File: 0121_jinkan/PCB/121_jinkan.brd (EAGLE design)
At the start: 25.4 x 33 mm, 16 parts

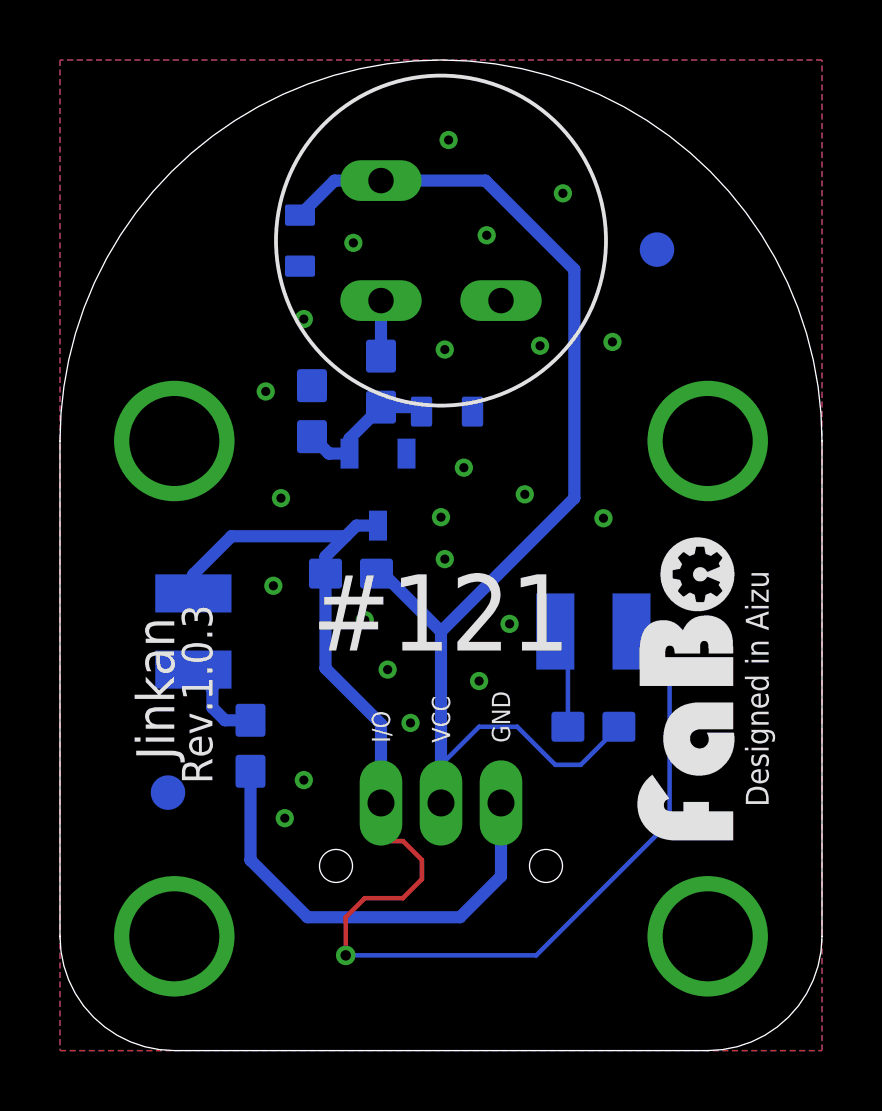
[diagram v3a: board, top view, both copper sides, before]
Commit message: #0121 Jinkan 配線太さ変更修正
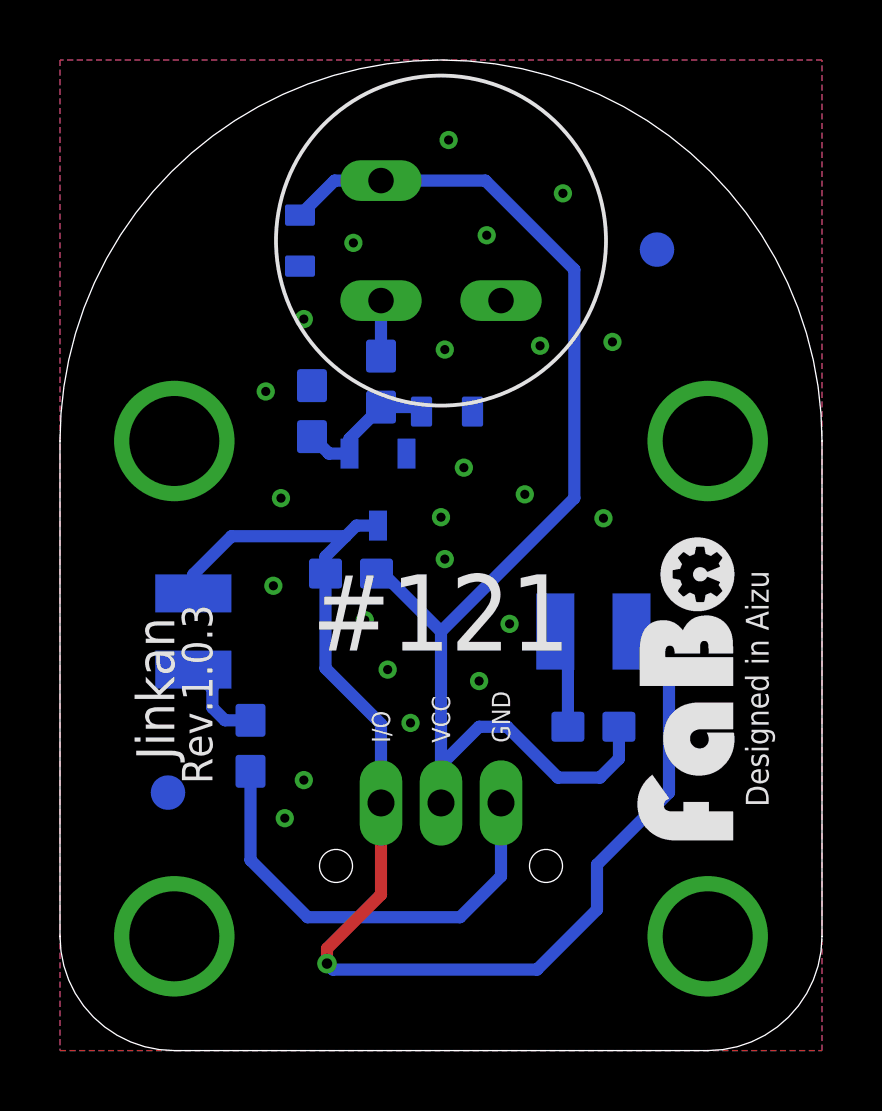
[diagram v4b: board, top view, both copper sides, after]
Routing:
- net VCC: track 42.2 -> 43.2 mm
- net I/O: track 44.7 -> 44.2 mm
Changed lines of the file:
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@@
 <rectangle x1="15.5" y1="15.3" x2="17.2" y2="15.6" layer="42"/>
 <rectangle x1="18.3" y1="15.3" x2="19.9" y2="15.6" layer="42"/>
-<rectangle x1="15.8" y1="12.4" x2="16.8" y2="12.6" layer="42"/>
+<rectangle x1="15.6" y1="12.4" x2="16.6" y2="12.6" layer="42"/>
 <rectangle x1="18.5" y1="12.3" x2="19.5" y2="12.6" layer="42"/>
 </plain>
@@
 <wire x1="5.715" y1="17.145" x2="9.525" y2="17.145" width="0.4064" layer="16"/>
 <contactref element="SJ2" pad="1"/>
-<wire x1="19.05" y1="13.97" x2="20.32" y2="12.7" width="0.1524" layer="16"/>
-<wire x1="15.875" y1="3.175" x2="9.525" y2="3.175" width="0.1524" layer="16"/>
-<via x="9.525" y="3.175" extent="1-16" drill="0.35"/>
-<wire x1="9.525" y1="3.175" x2="9.525" y2="4.445" width="0.1524" layer="1"/>
-<wire x1="9.525" y1="4.445" x2="10.16" y2="5.08" width="0.1524" layer="1"/>
-<wire x1="10.16" y1="5.08" x2="11.43" y2="5.08" width="0.1524" layer="1"/>
-<wire x1="11.43" y1="5.08" x2="12.065" y2="5.715" width="0.1524" layer="1"/>
-<wire x1="12.065" y1="5.715" x2="12.065" y2="6.35" width="0.1524" layer="1"/>
-<wire x1="12.065" y1="6.35" x2="11.43" y2="6.985" width="0.1524" layer="1"/>
-<wire x1="11.43" y1="6.985" x2="10.795" y2="6.985" width="0.1524" layer="1"/>
-<wire x1="10.795" y1="6.985" x2="10.7" y2="7.08" width="0.1524" layer="1"/>
-<wire x1="10.7" y1="7.08" x2="10.7" y2="8.255" width="0.1524" layer="1"/>
-<wire x1="20.32" y1="12.7" x2="20.32" y2="7.62" width="0.1524" layer="16"/>
-<wire x1="20.32" y1="7.62" x2="15.875" y2="3.175" width="0.1524" layer="16"/>
+<wire x1="19.05" y1="13.97" x2="20.3" y2="12.72" width="0.4064" layer="16"/>
+<wire x1="17.9" y1="4.7" x2="15.9" y2="2.7" width="0.4064" layer="16"/>
+<wire x1="15.9" y1="2.7" x2="9.1" y2="2.7" width="0.4064" layer="16"/>
+<wire x1="9.1" y1="2.7" x2="8.9" y2="2.9" width="0.4064" layer="16"/>
+<via x="8.9" y="2.9" extent="1-16" drill="0.35"/>
+<wire x1="8.9" y1="2.9" x2="8.9" y2="3.4" width="0.4064" layer="1"/>
+<wire x1="20.3" y1="12.72" x2="20.3" y2="8.6" width="0.4064" layer="16"/>
+<wire x1="20.3" y1="8.6" x2="17.9" y2="6.2" width="0.4064" layer="16"/>
+<wire x1="17.9" y1="6.2" x2="17.9" y2="4.7" width="0.4064" layer="16"/>
+<wire x1="8.9" y1="3.4" x2="10.7" y2="5.2" width="0.4064" layer="1"/>
+<wire x1="10.7" y1="5.2" x2="10.7" y2="8.255" width="0.4064" layer="1"/>
 </signal>
 <signal name="VCC">
@@
 <contactref element="R5" pad="2"/>
 <contactref element="R3" pad="2"/>
-<wire x1="18.63" y1="10.795" x2="17.36" y2="9.525" width="0.1524" layer="16"/>
-<wire x1="17.36" y1="9.525" x2="16.51" y2="9.525" width="0.1524" layer="16"/>
-<wire x1="16.51" y1="9.525" x2="15.24" y2="10.795" width="0.1524" layer="16"/>
-<wire x1="15.24" y1="10.795" x2="13.97" y2="10.795" width="0.1524" layer="16"/>
 <wire x1="12.7" y1="9.525" x2="12.7" y2="8.255" width="0.1524" layer="16"/>
-<wire x1="13.97" y1="10.795" x2="12.7" y2="9.525" width="0.1524" layer="16"/>
+<wire x1="12.7" y1="9.525" x2="13.97" y2="10.795" width="0.4064" layer="16"/>
 <wire x1="10.55" y1="15.9" x2="10.77" y2="15.9" width="0.4064" layer="16"/>
 <wire x1="10.77" y1="15.9" x2="12.7" y2="13.97" width="0.4064" layer="16"/>
+<wire x1="13.97" y1="10.795" x2="14.905" y2="10.795" width="0.4064" layer="16"/>
+<wire x1="14.905" y1="10.795" x2="16.6" y2="9.1" width="0.4064" layer="16"/>
+<wire x1="16.6" y1="9.1" x2="18" y2="9.1" width="0.4064" layer="16"/>
+<wire x1="18.63" y1="9.73" x2="18.63" y2="10.795" width="0.4064" layer="16"/>
+<wire x1="18" y1="9.1" x2="18.63" y2="9.73" width="0.4064" layer="16"/>
 </signal>
 <signal name="N$1">
@@
 <contactref element="SJ2" pad="2"/>
 <contactref element="R5" pad="1"/>
-<wire x1="16.51" y1="13.97" x2="16.93" y2="13.55" width="0.1524" layer="16"/>
-<wire x1="16.93" y1="13.55" x2="16.93" y2="10.795" width="0.1524" layer="16"/>
+<wire x1="16.51" y1="13.97" x2="16.93" y2="13.55" width="0.4064" layer="16"/>
+<wire x1="16.93" y1="13.55" x2="16.93" y2="10.795" width="0.4064" layer="16"/>
 </signal>
 </signals>
